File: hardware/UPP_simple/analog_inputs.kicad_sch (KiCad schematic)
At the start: 138 parts, among them J10 Conn_01x04, J11 Conn_01x04, J12 Conn_01x04, J13 Conn_01x04, J14 Conn_01x04, J3 Conn_01x03, J4 Conn_01x03, J5 Conn_01x03, J6 Conn_01x03, J7 Conn_01x03, J8 Conn_01x03, J9 Conn_01x04, U7 Opamp_Quad, U8 Opamp_Quad, U9 Opamp_Quad

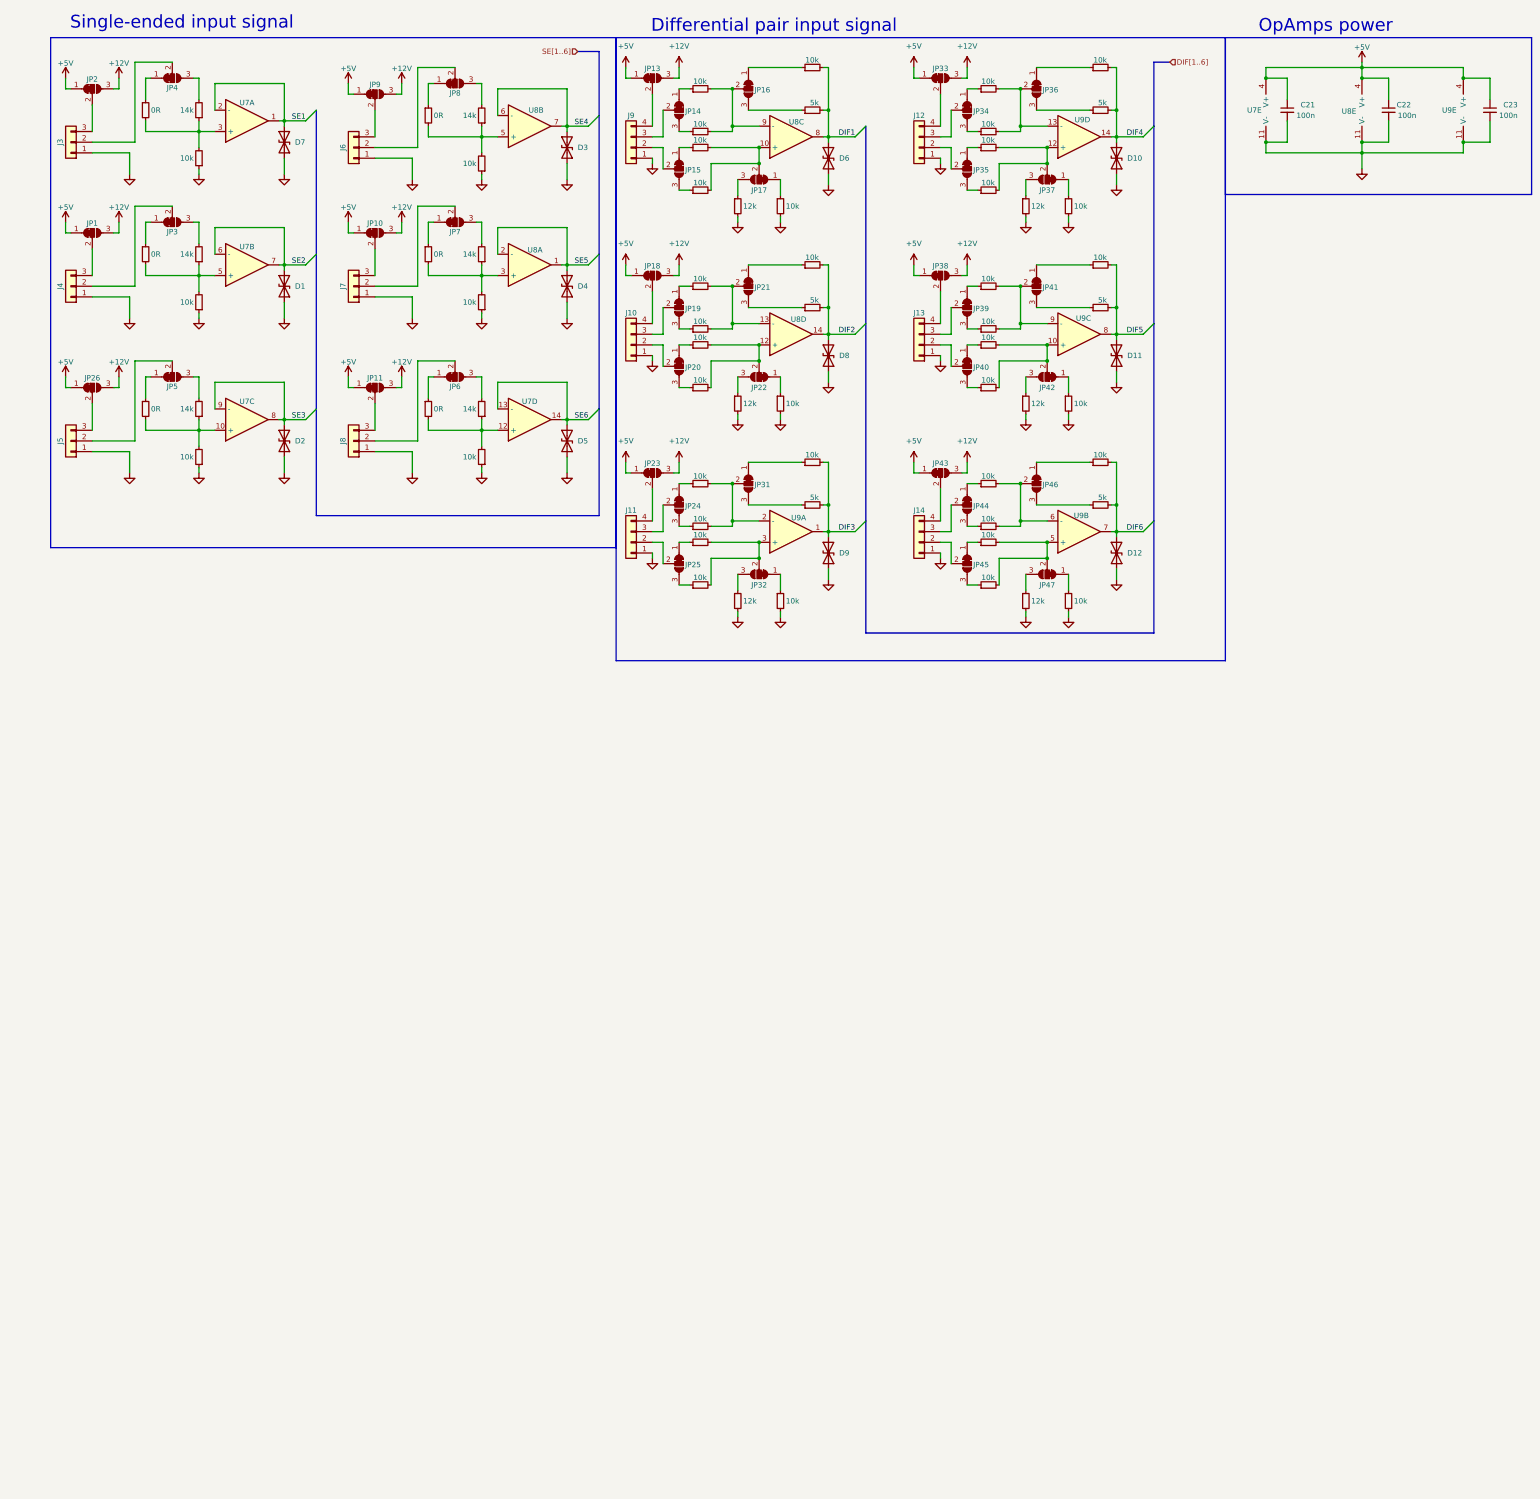
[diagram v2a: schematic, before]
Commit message: Changed Opamps cleared schematic
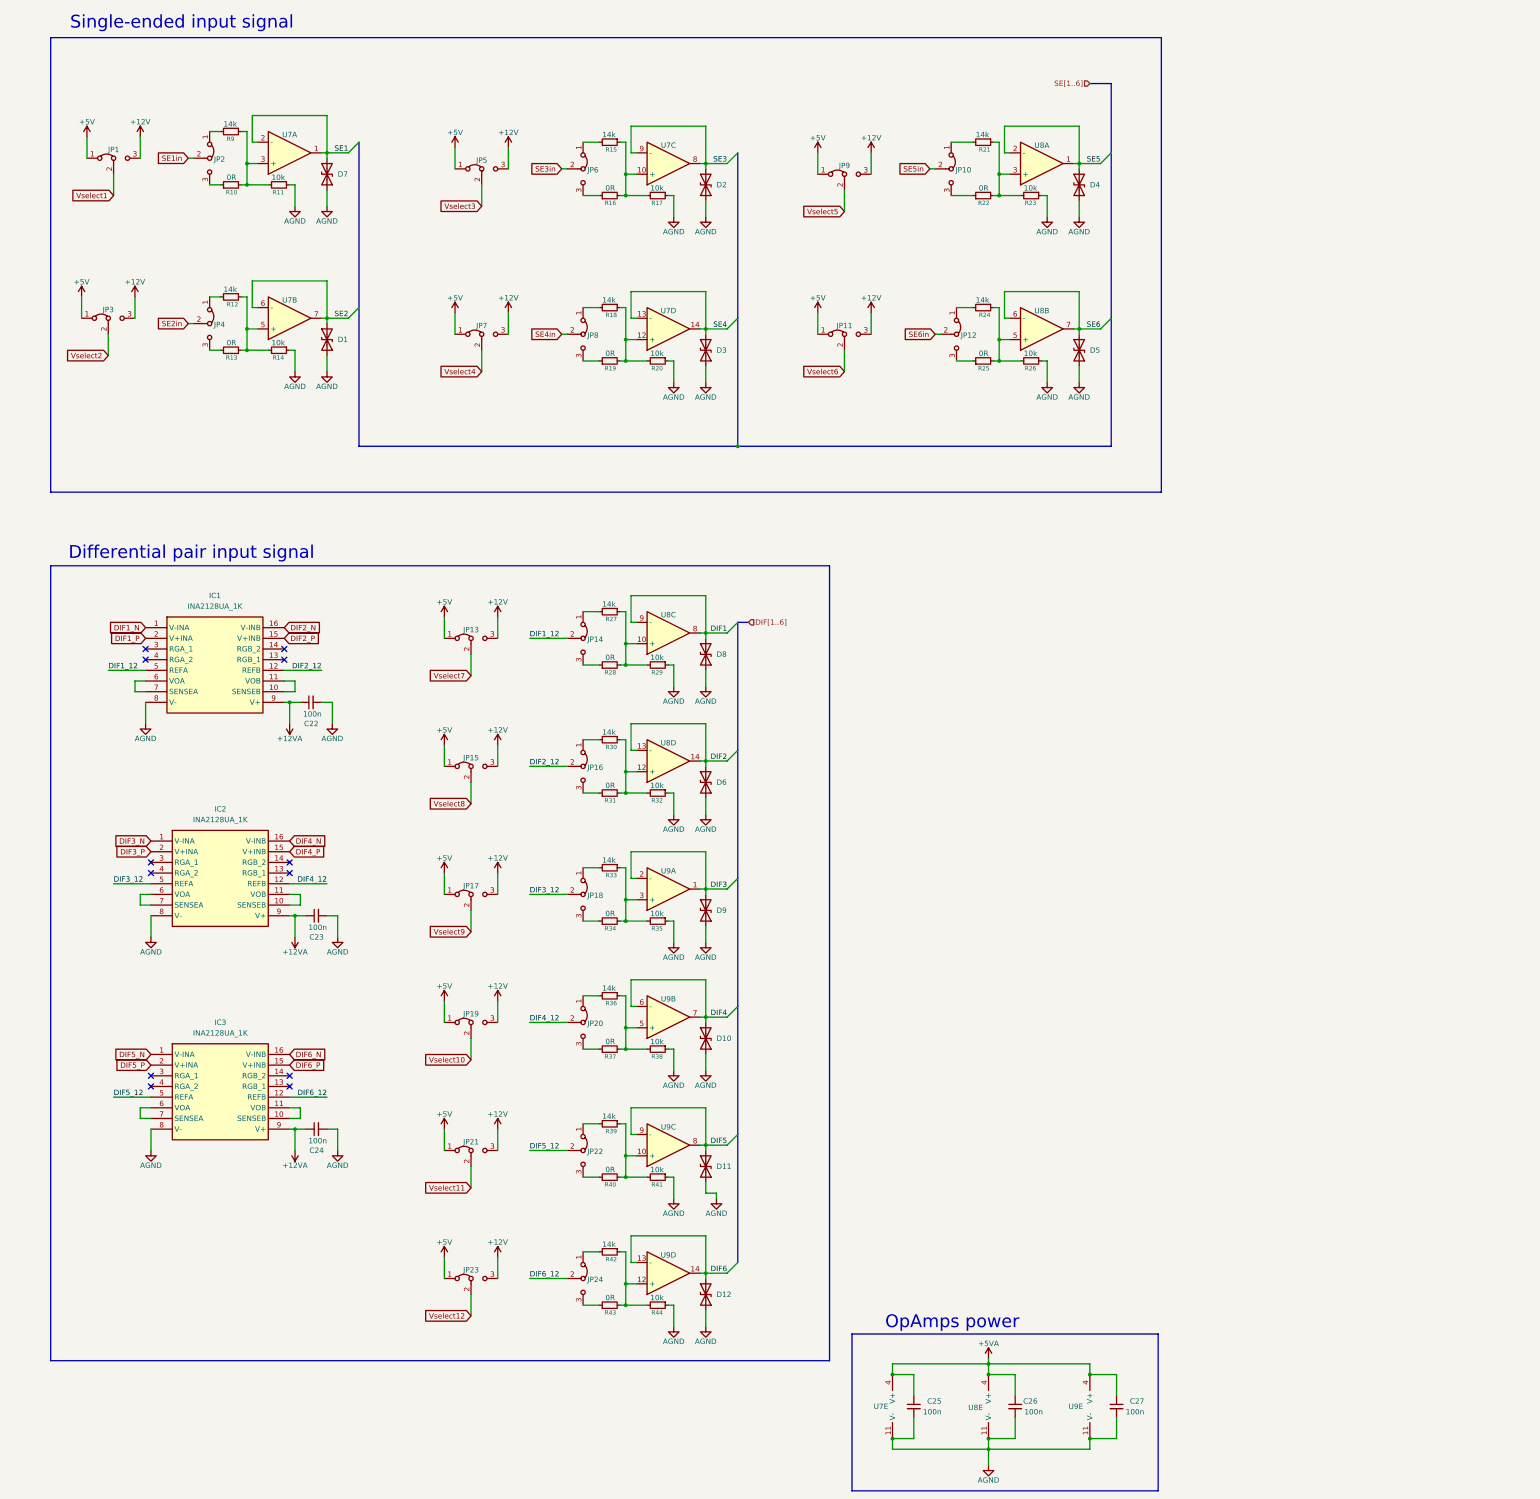
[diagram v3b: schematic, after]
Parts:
- removed J10, J11, J12, J13, J14, J9: Conn_01x04, symbol Connector_Generic:Conn_01x04
- removed J3, J4, J5, J6, J7, J8: Conn_01x03, symbol Connector_Generic:Conn_01x03
- removed JP1, JP10, JP11, JP13, JP14, JP15, JP16, JP17, JP18, JP19, JP2, JP20, JP21, JP22, JP23, JP24, JP25, JP26, JP3, JP31, JP32, JP33, JP34, JP35, JP36, JP37, JP38, JP39, JP4, JP40, JP41, JP42, JP43, JP44, JP45, JP46, JP47, JP5, JP6, JP7, JP8, JP9: SolderJumper_3_Bridged12, Jumper:SolderJumper-3_P1.3mm_Bridged12_Pad1.0x1.5mm, symbol Jumper:SolderJumper_3_Bridged12
- removed R1, R4, R7: 0R, Resistor_SMD:R_0603_1608Metric_Pad0.98x0.95mm_HandSolder, symbol Device:R_Small
- removed R2, R5: 14k, Resistor_SMD:R_0603_1608Metric_Pad0.98x0.95mm_HandSolder, symbol Device:R_Small
- removed R3, R45, R47, R48, R50, R51, R52, R53, R55, R6, R64, R66, R67, R68, R69, R71, R72, R74, R75, R76, R77, R79, R8, R80: 10k, Resistor_SMD:R_0603_1608Metric_Pad0.98x0.95mm_HandSolder, symbol Device:R_Small
- removed R46, R54, R70, R78: 12k, Resistor_SMD:R_0603_1608Metric_Pad0.98x0.95mm_HandSolder, symbol Device:R_Small
- removed R49, R65, R73, R81: 5k, Resistor_SMD:R_0603_1608Metric_Pad0.98x0.95mm_HandSolder, symbol Device:R_Small
- added C22, C23, C24: 100n, Capacitor_SMD:C_0603_1608Metric, symbol Device:C_Small
- added IC1, IC2, IC3: INA2128UA_1K, SOIC127P1030X265-16N, symbol INA2128UA_1K:INA2128UA_1K
- added JP1, JP10, JP11, JP12, JP13, JP14, JP15, JP16, JP17, JP18, JP19, JP2, JP20, JP21, JP22, JP23, JP24, JP3, JP4, JP5, JP6, JP7, JP8, JP9: Jumper_3_Bridged12, Connector_PinHeader_1.00mm:PinHeader_1x03_P1.00mm_Vertical, symbol Jumper:Jumper_3_Bridged12
- added R12, R15, R18, R33: 14k, Resistor_SMD:R_0603_1608Metric_Pad0.98x0.95mm_HandSolder, symbol Device:R_Small
- added R13: 0R, Resistor_SMD:R_0603_1608Metric_Pad0.98x0.95mm_HandSolder, symbol Device:R_Small
- added R14, R17: 10k, Resistor_SMD:R_0603_1608Metric_Pad0.98x0.95mm_HandSolder, symbol Device:R_Small
- R16: value 14k -> 0R
- R19, R22, R25, R28, R31, R34, R37, R40, R43: value 10k -> 0R
- R20, R23: value 0R -> 10k
- R27, R30, R36, R39, R42: value 10k -> 14k
- R29, R38: value 12k -> 10k
- R32, R41: value 5k -> 10k
- renumbered C21 to C25, C22 to C26, C23 to C27, R33 to R10, R18 to R11, R17 to R9
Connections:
- net +12V: now also JP1.3 (B), JP11.3 (B), JP13.3 (B), JP15.3 (B), JP17.3 (B), JP19.3 (B), JP21.3 (B), JP23.3 (B), JP3.3 (B), JP5.3 (B), JP7.3 (B), JP9.3 (B)
- net +5V: now also JP1.1 (A), JP11.1 (A), JP13.1 (A), JP15.1 (A), JP17.1 (A), JP19.1 (A), JP21.1 (A), JP23.1 (A), JP3.1 (A), JP5.1 (A), JP7.1 (A), JP9.1 (A); no longer C25.1, C26.1, C27.1, U7.4 (V+), U8.4 (V+), U9.4 (V+)
- net DIF1: now also D8.2 (A2), U8.9 (-); no longer D6.2 (A2), R31.2, R32.2
- net DIF2: now also D6.2 (A2), U8.13 (-); no longer D8.2 (A2), R40.2, R41.2
- net DIF3: now also U9.2 (-)
- net DIF4: now also U9.6 (-), U9.7; no longer U9.14
- net DIF5: now also U9.9 (-)
- net DIF6: now also U9.13 (-), U9.14; no longer U9.7
- net SE4: now also U7.13 (-), U7.14; no longer U8.6 (-), U8.7
- net SE6: now also U8.6 (-), U8.7; no longer U7.13 (-), U7.14
- net at U7.5 (+): now also R12.1, R13.2, R14.2
- net AGND: now reaches R20.1
- net AGND: now also C25.2, C26.2, C27.2, D1.1 (A1), D10.1 (A1), D11.1 (A1), D12.1 (A1), D2.1 (A1), D3.1 (A1), D4.1 (A1), D5.1 (A1), D6.1 (A1), D7.1 (A1), D8.1 (A1), D9.1 (A1), R11.1, R23.1, R26.1, R29.1, R32.1, R35.1, R38.1, R41.1, R44.1, U7.11 (V-), U8.11 (V-), U9.11 (V-), C22.2, C23.2, C24.2, IC1.8 (V-), IC2.8 (V-), IC3.8 (V-), R14.1, R17.1
- net at R21.2: now also JP10.1 (A)
- net at R44.2: now also R42.1, R43.2, U9.12 (+); no longer U9.3 (+)
- net at U9.5 (+): now also R36.1, R37.2, R38.2
- net at R24.2: now also JP12.1 (A)
- net at R39.1: now also R40.2, R41.2, U9.10 (+)
- net at R16.2: now also U7.10 (+), R15.1, R17.2
- net at R37.1: now also JP20.3 (B)
- net at R28.1: now also JP14.3 (B)
- net at R28.2, U8.10 (+): now also R27.1, R29.2; no longer R27.2
- net at R34.1: now also JP18.3 (B)
- net at R34.2, R35.2: now also U9.3 (+), R33.1; no longer U8.13 (-)
- net at R31.1: now also JP16.3 (B)
- net at R30.1: now also R31.2, R32.2, U8.12 (+)
- net at R40.1: now also JP22.3 (B)
- net at R26.2: now also R24.1, R25.2, U8.5 (+); no longer U8.9 (-)
- net at R10.1: now also JP2.3 (B)
- net at R21.1, R22.2, U8.3 (+): now also R23.2; no longer R20.2
- net at R9.2: now also JP2.1 (A)
- net at R43.1: now also JP24.3 (B)
- removed net GND: C25.2, C26.2, C27.2, D1.1 (A1), D10.1 (A1), D11.1 (A1), D12.1 (A1), D2.1 (A1), D3.1 (A1), D4.1 (A1), D5.1 (A1), D6.1 (A1), D7.1 (A1), D8.1 (A1), D9.1 (A1), R11.1, R19.1, R22.1, R25.1, R29.2, R30.2, R38.2, R39.2, U7.11 (V-), U8.11 (V-), U9.11 (V-)
- new net: JP10.3 (B), R22.1
- new net: JP4.3 (B), R13.1
- new net: JP6.1 (A), R15.2
- new net: JP6.3 (B), R16.1
- new net: IC3.10 (SENSEB), IC3.11 (VOB)
- new net: IC3.6 (VOA), IC3.7 (SENSEA)
- new net: JP16.1 (A), R30.2
- new net: JP14.1 (A), R27.2
- new net: JP18.1 (A), R33.2
- new net: JP12.3 (B), R25.1
- new net: IC2.10 (SENSEB), IC2.11 (VOB)
- new net: IC2.6 (VOA), IC2.7 (SENSEA)
- new net: JP8.3 (B), R19.1
- new net: R18.1, R19.2, R20.2, U7.12 (+)
- new net: JP8.1 (A), R18.2
- new net: JP24.1 (A), R42.2
- new net: JP22.1 (A), R39.2
- new net: JP4.1 (A), R12.2
- new net: IC1.10 (SENSEB), IC1.11 (VOB)
- new net: IC1.6 (VOA), IC1.7 (SENSEA)
- new net: JP20.1 (A), R36.2
- new net +12VA: C22.1, C23.1, C24.1, IC1.9 (V+), IC2.9 (V+), IC3.9 (V+)
- new net +5VA: C25.1, C26.1, C27.1, U7.4 (V+), U8.4 (V+), U9.4 (V+)
- new net DIF1_12: IC1.5 (REFA), JP14.2 (C)
- new net DIF1_N: IC1.1 (V-INA)
- new net DIF1_P: IC1.2 (V+INA)
- new net DIF2_12: IC1.12 (REFB), JP16.2 (C)
- new net DIF2_N: IC1.16 (V-INB)
- new net DIF2_P: IC1.15 (V+INB)
- new net DIF3_12: IC2.5 (REFA), JP18.2 (C)
- new net DIF3_N: IC2.1 (V-INA)
- new net DIF3_P: IC2.2 (V+INA)
- new net DIF4_12: IC2.12 (REFB), JP20.2 (C)
- new net DIF4_N: IC2.16 (V-INB)
- new net DIF4_P: IC2.15 (V+INB)
- new net DIF5_12: IC3.5 (REFA), JP22.2 (C)
- new net DIF5_N: IC3.1 (V-INA)
- new net DIF5_P: IC3.2 (V+INA)
- new net DIF6_12: IC3.12 (REFB), JP24.2 (C)
- new net DIF6_N: IC3.16 (V-INB)
- new net DIF6_P: IC3.15 (V+INB)
- new net SE1in: JP2.2 (C)
- new net SE2in: JP4.2 (C)
- new net SE3in: JP6.2 (C)
- new net SE4in: JP8.2 (C)
- new net SE5in: JP10.2 (C)
- new net SE6in: JP12.2 (C)
- new net Vselect1: JP1.2 (C)
- new net Vselect10: JP19.2 (C)
- new net Vselect11: JP21.2 (C)
- new net Vselect12: JP23.2 (C)
- new net Vselect2: JP3.2 (C)
- new net Vselect3: JP5.2 (C)
- new net Vselect4: JP7.2 (C)
- new net Vselect5: JP9.2 (C)
- new net Vselect6: JP11.2 (C)
- new net Vselect7: JP13.2 (C)
- new net Vselect8: JP15.2 (C)
- new net Vselect9: JP17.2 (C)
- no-connect marks 0 -> 12
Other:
- title: Universal use measuring PCB -> Universal Measurement Board
- moved on the sheet: C25, C26, C27, D7, U7A, U7E, U8E, U9E
